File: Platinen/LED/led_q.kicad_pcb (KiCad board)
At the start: 2 copper layers, 3 parts, among them P1 CONN_2

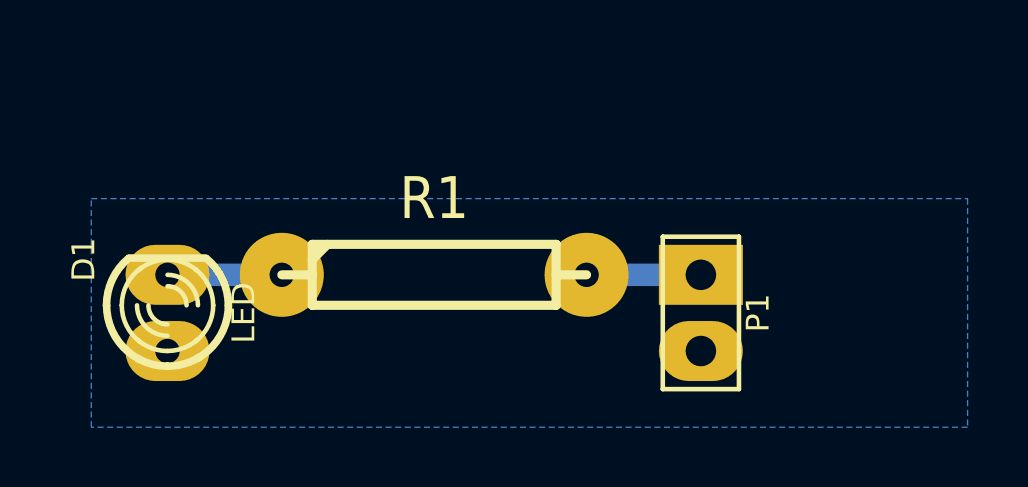
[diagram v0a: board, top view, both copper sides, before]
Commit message: Platinen auf den neusten Stand gebracht und alternatives Layout bei der LED
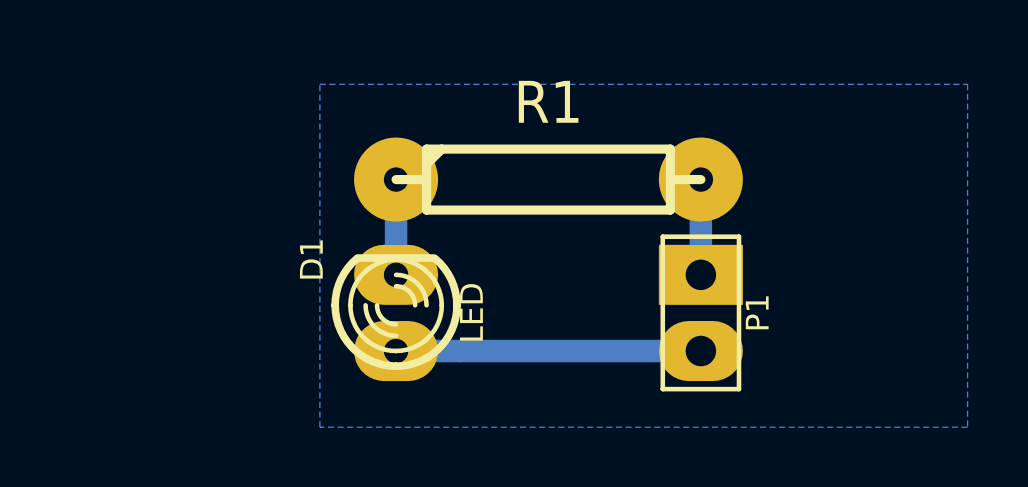
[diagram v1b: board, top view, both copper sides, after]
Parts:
- moved D1 7.62 mm to (59.7, 50.8)
- moved R1 4.96 mm to (64.8, 46.4)
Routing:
- net N-000001: track 0.00 -> 10.2 mm
- net N-000002: track 3.81 -> 3.18 mm
- net N-000003: track 3.81 -> 3.18 mm
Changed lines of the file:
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@@
     (thickness 1.6)
     (drawings 4)
-    (tracks 2)
+    (tracks 4)
     (zones 0)
     (modules 3)
@@
     (pad_to_mask_clearance 0)
     (solder_mask_min_width 0.25)
-    (aux_axis_origin 49.53 54.61)
-    (grid_origin 45.72 55.88)
+    (aux_axis_origin 57.15 54.61)
+    (grid_origin 57.15 54.61)
     (visible_elements FFFFFFBF)
     (pcbplotparams
@@
   )
   (module R4 (layer F.Cu)
-    (at 60.96 49.53)
+    (at 64.77 46.355)
     (descr "Resitance 4 pas")
     (tags R)
@@
   )
   (module LED-3MM (layer F.Cu)
-    (at 52.07 50.8 90)
+    (at 59.69 50.8 90)
     (descr "LED 3mm - Lead pitch 100mil (2,54mm)")
     (tags "LED led 3mm 3MM 100mil 2,54mm")
@@
     )
   )
-  (dimension 7.62 (width 0.25) (layer F.Adhes)
-    (gr_text "7,620 mm" (at 45.49 50.8 270) (layer F.Adhes)
+  (dimension 11.43 (width 0.25) (layer F.Adhes)
+    (gr_text "11,430 mm" (at 53.11 48.895 270) (layer F.Adhes)
       (effects (font (size 1 1) (thickness 0.25)))
     )
-    (feature1 (pts (xy 48.26 54.61) (xy 46.403579 54.61)))
-    (feature2 (pts (xy 48.26 46.99) (xy 46.403579 46.99)))
-    (crossbar (pts (xy 46.99 46.99) (xy 46.99 54.61)))
-    (arrow1a (pts (xy 46.99 54.61) (xy 46.403579 53.483496)))
-    (arrow1b (pts (xy 46.99 54.61) (xy 47.576421 53.483496)))
-    (arrow2a (pts (xy 46.99 46.99) (xy 46.403579 48.116504)))
-    (arrow2b (pts (xy 46.99 46.99) (xy 47.576421 48.116504)))
-  )
-  (dimension 29.21 (width 0.25) (layer F.Adhes)
-    (gr_text "29,210 mm" (at 64.282744 43.647673) (layer F.Adhes)
+    (feature1 (pts (xy 55.88 54.61) (xy 54.023579 54.61)))
+    (feature2 (pts (xy 55.88 43.18) (xy 54.023579 43.18)))
+    (crossbar (pts (xy 54.61 43.18) (xy 54.61 54.61)))
+    (arrow1a (pts (xy 54.61 54.61) (xy 54.023579 53.483496)))
+    (arrow1b (pts (xy 54.61 54.61) (xy 55.196421 53.483496)))
+    (arrow2a (pts (xy 54.61 43.18) (xy 54.023579 44.306504)))
+    (arrow2b (pts (xy 54.61 43.18) (xy 55.196421 44.306504)))
+  )
+  (dimension 21.59 (width 0.25) (layer F.Adhes)
+    (gr_text "21,590 mm" (at 67.945 39.14) (layer F.Adhes)
       (effects (font (size 1 1) (thickness 0.25)))
     )
-    (feature1 (pts (xy 78.887744 46.417673) (xy 78.887744 44.561252)))
-    (feature2 (pts (xy 49.677744 46.417673) (xy 49.677744 44.561252)))
-    (crossbar (pts (xy 49.677744 45.147673) (xy 78.887744 45.147673)))
-    (arrow1a (pts (xy 78.887744 45.147673) (xy 77.76124 45.734094)))
-    (arrow1b (pts (xy 78.887744 45.147673) (xy 77.76124 44.561252)))
-    (arrow2a (pts (xy 49.677744 45.147673) (xy 50.804248 45.734094)))
-    (arrow2b (pts (xy 49.677744 45.147673) (xy 50.804248 44.561252)))
+    (feature1 (pts (xy 78.74 41.91) (xy 78.74 40.053579)))
+    (feature2 (pts (xy 57.15 41.91) (xy 57.15 40.053579)))
+    (crossbar (pts (xy 57.15 40.64) (xy 78.74 40.64)))
+    (arrow1a (pts (xy 78.74 40.64) (xy 77.613496 41.226421)))
+    (arrow1b (pts (xy 78.74 40.64) (xy 77.613496 40.053579)))
+    (arrow2a (pts (xy 57.15 40.64) (xy 58.276504 41.226421)))
+    (arrow2b (pts (xy 57.15 40.64) (xy 58.276504 40.053579)))
   )
   (gr_text PIN (at 72.39 49.53) (layer F.Paste)
@@
     (effects (font (size 1.8 1.8) (thickness 0.1)) (justify left))
   )
-  (segment (start 55.88 49.53) (end 52.07 49.53) (width 0.75) (layer B.Cu) (net 2))
-  (segment (start 69.85 49.53) (end 66.04 49.53) (width 0.75) (layer B.Cu) (net 3) (status 30))
+  (segment (start 61.84 52.07) (end 69.85 52.07) (width 0.75) (layer B.Cu) (net 1))
+  (segment (start 59.69 52.07) (end 61.84 52.07) (width 0.75) (layer B.Cu) (net 1))
+  (segment (start 59.69 46.355) (end 59.69 49.53) (width 0.75) (layer B.Cu) (net 2))
+  (segment (start 69.85 46.355) (end 69.85 49.53) (width 0.75) (layer B.Cu) (net 3))
   (zone (net 1) (net_name N-000001) (layer B.Cu) (hatch edge 0.508)
     (connect_pads (clearance 0.8))
@@
     (polygon
       (pts
-        (xy 78.74 54.61) (xy 49.53 54.61) (xy 49.53 46.99) (xy 78.74 46.99)
+        (xy 78.74 54.61) (xy 57.15 54.61) (xy 57.15 43.18) (xy 78.74 43.18)
       )
     )
